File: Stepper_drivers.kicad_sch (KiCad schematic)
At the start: 11 parts, among them J7 Conn_01x04_Socket, J8 Conn_01x02_Socket, U4 ADUM1201ARZ, U5 ADUM1201ARZ, U6 HT26LS31ARZ

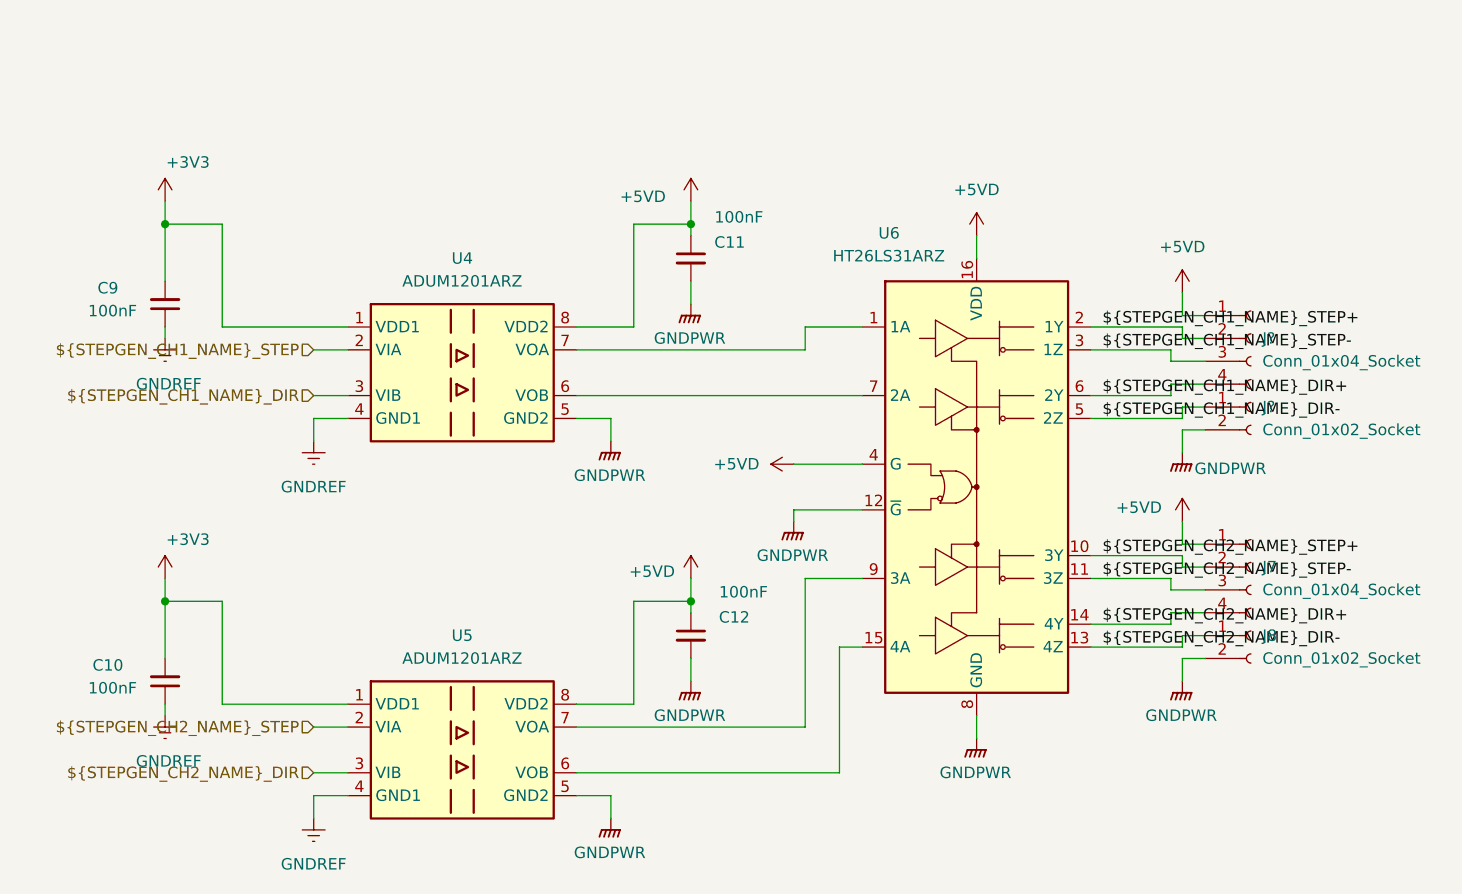
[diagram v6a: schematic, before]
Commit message: Swapped out stepper isolators to use same as others. further BOM consolidation. Fixed bug with incorrect differential driver footprint.
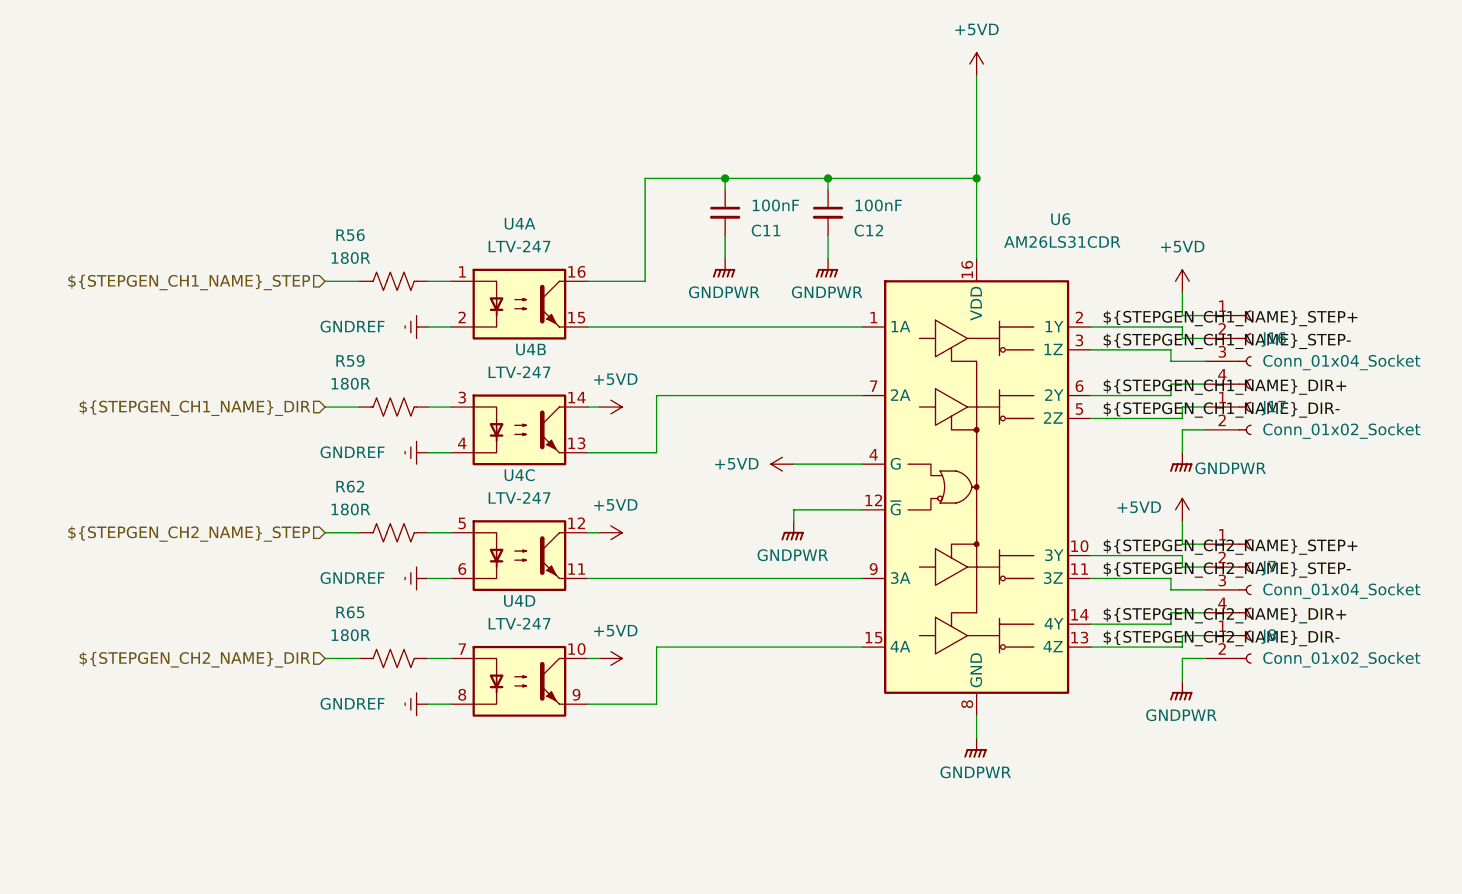
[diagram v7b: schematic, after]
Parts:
- removed C10, C9: 100nF, Capacitor_SMD:C_1206_3216Metric_Pad1.33x1.80mm_HandSolder, symbol Device:C_Small
- removed U4, U5: ADUM1201ARZ, Package_SO:SOIC-8_3.9x4.9mm_P1.27mm, symbol Isolator:ADuM1200AR
- added R56, R59, R62, R65: 180R, Resistor_SMD:R_1206_3216Metric_Pad1.30x1.75mm_HandSolder, symbol Device:R_US
- added U4: LTV-247, Package_SO:SOP-16_4.4x10.4mm_P1.27mm, symbol Isolator:LTV-247
- C11, C12: Digikey Part Number (none) -> 399-C1206C104K5RACTUCT-ND; Digikey URL (none) -> https://www.digikey.com.au/en/products/detail/kemet/C1206C1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
- U6: value HT26LS31ARZ -> AM26LS31CDR; footprint Package_DIP:SMDIP-4_W9.53mm -> Package_SO:SOIC-16_3.9x9.9mm_P1.27mm
- gave numbers to parts that had none: 2
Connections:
- net ${STEPGEN_CH1_NAME}_DIR: now also R59.1
- net ${STEPGEN_CH1_NAME}_STEP: now also R56.1
- net ${STEPGEN_CH2_NAME}_DIR: now also R65.1
- net ${STEPGEN_CH2_NAME}_STEP: now also R62.1
- net +5VD: now also U4.10, U4.12, U4.14, U4.16
- net GNDREF: now also U4.2, U4.4, U4.6, U4.8
- net at U6.7 (2A): now also U4.13
- net at U6.1 (1A): now also U4.15
- net at U6.15 (4A): now also U4.9
- net at U6.9 (3A): now also U4.11
- new net: R56.2, U4.1
- new net: R59.2, U4.3
- new net: R62.2, U4.5
- new net: R65.2, U4.7
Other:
- moved on the sheet: C11

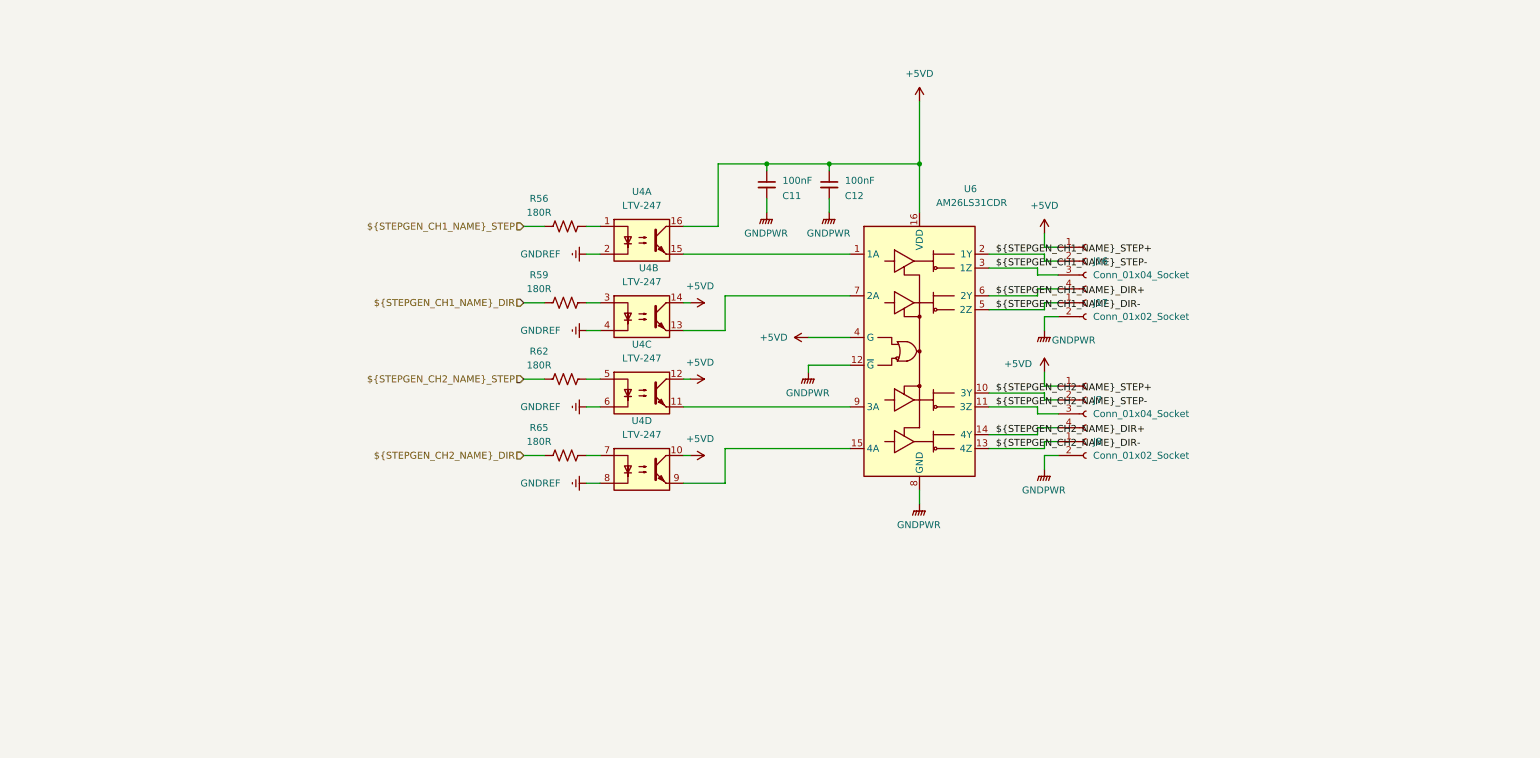
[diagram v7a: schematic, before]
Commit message: Built up stepper driver circuit on breadboard and tested up to 100khz, made some tweaks and happy to report this part of the design is now validated
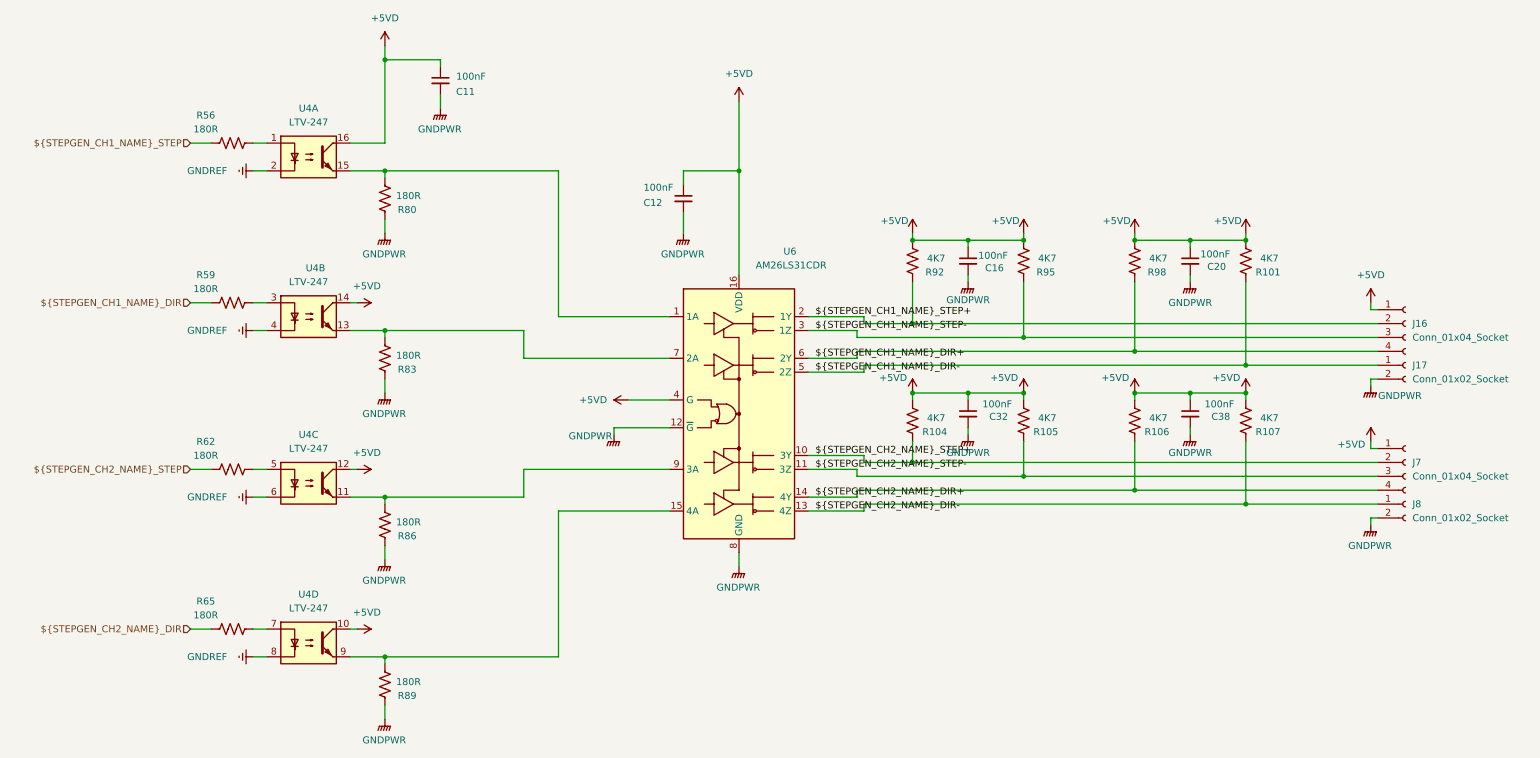
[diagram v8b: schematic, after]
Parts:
- added C16, C20, C32, C38: 100nF, Capacitor_SMD:C_1206_3216Metric_Pad1.33x1.80mm_HandSolder, symbol Device:C_Small
- added R101, R104, R105, R106, R107, R92, R95, R98: 4K7, Resistor_SMD:R_1206_3216Metric_Pad1.30x1.75mm_HandSolder, symbol Device:R_US
- added R80, R83, R86, R89: 180R, Resistor_SMD:R_1206_3216Metric_Pad1.30x1.75mm_HandSolder, symbol Device:R_US
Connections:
- net ${STEPGEN_CH1_NAME}_DIR+: now also R98.1
- net ${STEPGEN_CH1_NAME}_DIR-: now also R101.1
- net ${STEPGEN_CH1_NAME}_STEP+: now also R92.1
- net ${STEPGEN_CH1_NAME}_STEP-: now also R95.1
- net ${STEPGEN_CH2_NAME}_DIR+: now also R106.1
- net ${STEPGEN_CH2_NAME}_DIR-: now also R107.1
- net ${STEPGEN_CH2_NAME}_STEP+: now also R104.1
- net ${STEPGEN_CH2_NAME}_STEP-: now also R105.1
- net +5VD: now also C16.1, C20.1, C32.1, C38.1, R101.2, R104.2, R105.2, R106.2, R107.2, R92.2, R95.2, R98.2
- net GNDPWR: now also C16.2, C20.2, C32.2, C38.2, R80.1, R83.1, R86.1, R89.1
- net at U4.13, U6.7 (2A): now also R83.2
- net at U4.15, U6.1 (1A): now also R80.2
- net at U4.9, U6.15 (4A): now also R89.2
- net at U4.11, U6.9 (3A): now also R86.2
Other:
- moved on the sheet: C11, C12, J16, J17, J7, J8, R56, R59, R62, R65, U4A, U4B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
